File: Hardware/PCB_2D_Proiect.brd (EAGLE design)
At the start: 46 x 35 mm, 104 parts, among them IC1 BQ25180YBGR_BQ25180YBGR, IC2 DRV2605YZFR_DRV2605YZFR, IC3 BMA423_BMA423, IC9 RT6160AWSC_RT6160AWSC, J1 503480-2400_503480-2400, J2 TC2030-IDC_TC2030-IDC, J4 KH-TYPE-C-16P_KH-TYPE-C-16P, Q1 20V/4.2A/52mΩ/1.4W, Q3 ESP32_C6_LIBRARY_6_SI1308EDL-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, U1 NORDIC_NRF_4_NRF52840_QF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

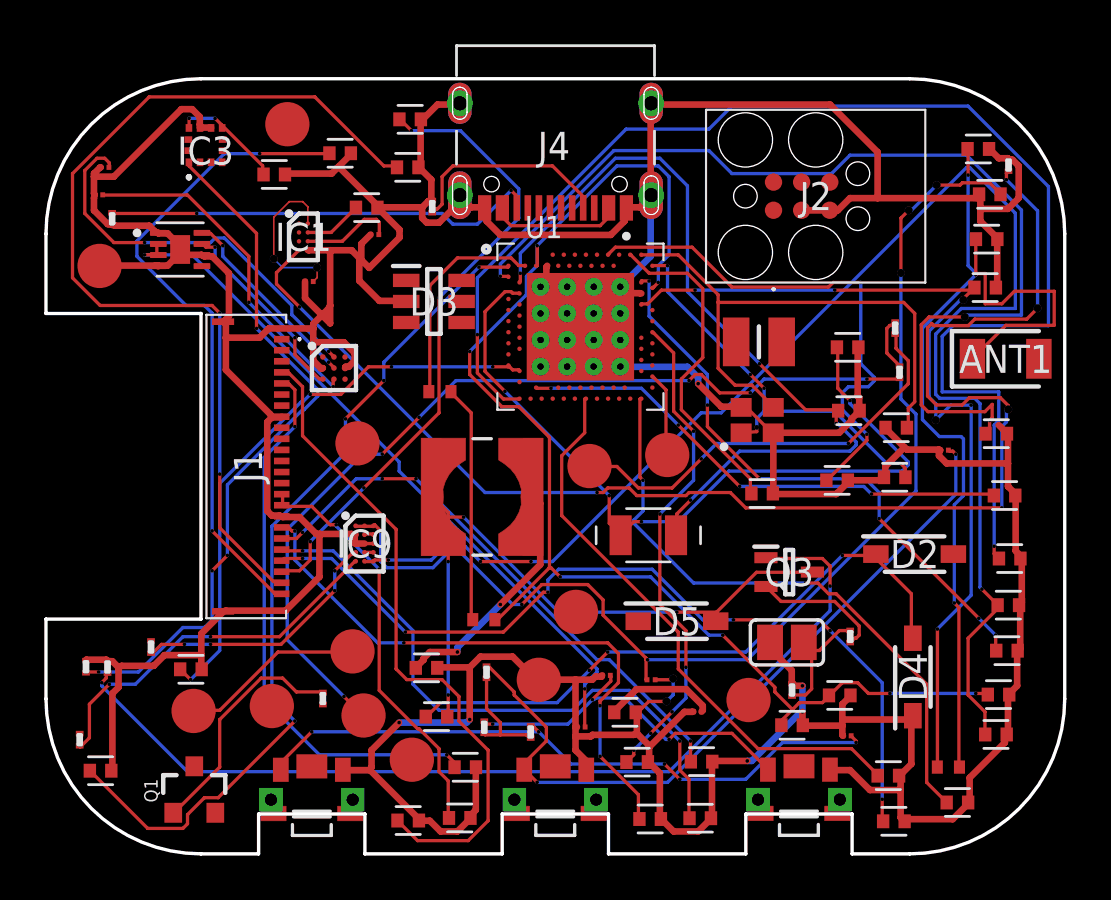
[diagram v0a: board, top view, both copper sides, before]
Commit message: fix antenna
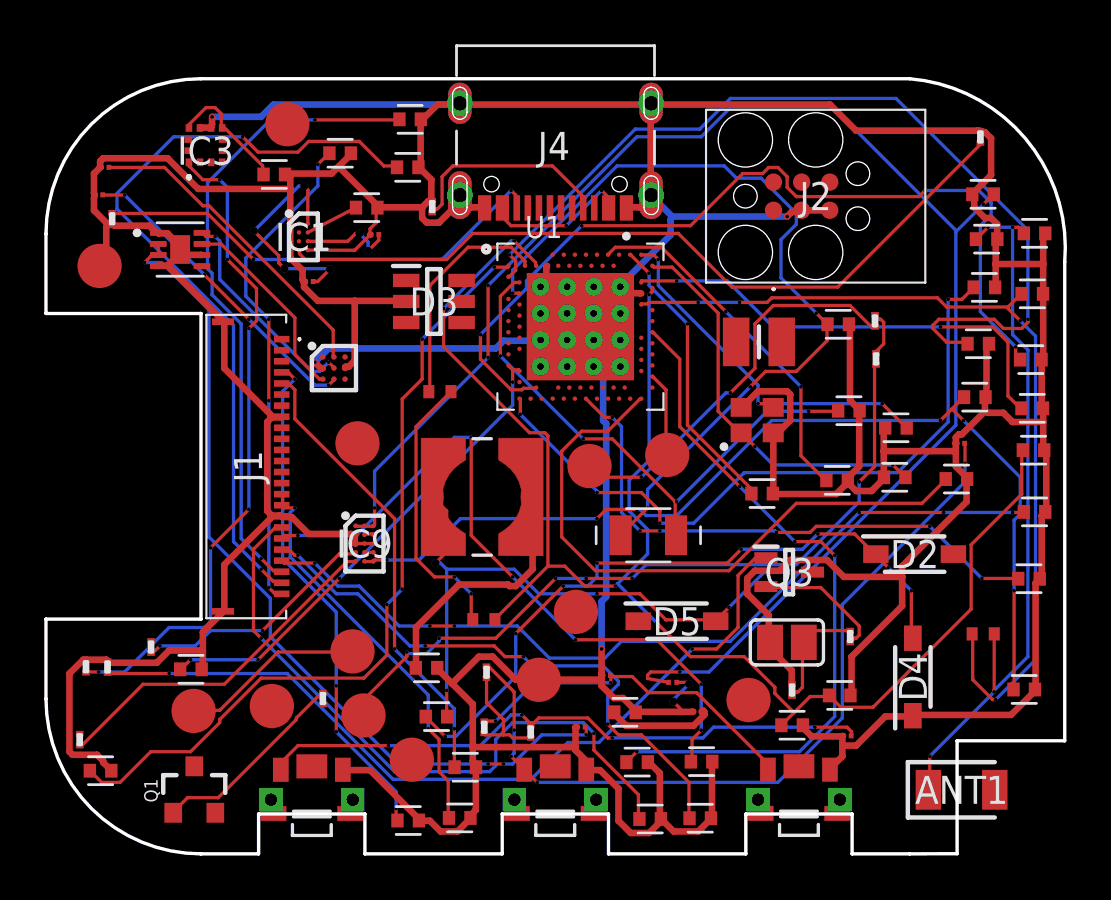
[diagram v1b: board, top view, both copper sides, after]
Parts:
- moved ANT1 19.6 mm to (19.2, -15.4)
- moved EPD_C9 15.3 mm to (22.5, -2.81)
- moved C8 14.6 mm to (18.9, -1.33)
- moved C21 12.3 mm to (20.2, 7.33)
- moved C10 11.1 mm to (22.4, -0.03)
- moved C11 11.0 mm to (22.4, 1.86)
- moved C7 10.9 mm to (22.2, -5.83)
- moved C25 9.51 mm to (19.8, 2.37)
- moved C20 6.25 mm to (22.3, 4.06)
- moved L1 6.21 mm to (20.1, -8.32)
- moved C4 4.58 mm to (22.5, 9.77)
- moved C5 4.14 mm to (19.9, 4.78)
- moved C33 2.40 mm to (22.0, -10.8)
- moved C3 2.15 mm to (22.4, 7.03)
- moved R9 1.80 mm to (20.0, 14.1)
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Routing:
- net GND: track 317.7 -> 366.0 mm, vias 8 -> 6
- net N$48: track 61.2 -> 31.3 mm, vias 2 -> 4
- net N$2: track 63.3 -> 35.3 mm, vias 6 -> 0
- net N$6: track 67.6 -> 44.4 mm, vias 4 -> 6
- net N$9: track 52.5 -> 71.5 mm, vias 6 -> 5
- net N$32: track 22.7 -> 39.8 mm
- net N$49: track 37.4 -> 25.0 mm
- net N$44: track 59.3 -> 71.5 mm, vias 7 -> 5
- net N$27: track 43.3 -> 32.7 mm, vias 3 -> 4
- net N$24: track 22.4 -> 31.7 mm, vias 6 -> 4
- net N$25: track 25.2 -> 17.1 mm, vias 0 -> 3
- net N$45: track 23.9 -> 16.2 mm
- net N$11: track 41.0 -> 33.6 mm
- net N$75: track 43.0 -> 35.5 mm
- net N$76: track 29.6 -> 22.3 mm, vias 2 -> 4
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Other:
- outline, holes or cut-outs redrawn
